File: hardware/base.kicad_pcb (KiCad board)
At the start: 4 copper layers, 100 x 85 mm, 296 parts, among them J101 USB-A, J102 TNG-Data-TOP, J103 TNG-Power-TOP, J301 MICROSDCARD, J302 Raspberry-Pi-Compute-Socket, J303 MICRO_HDMI, J304 USB Micro, J401 RJSLG-001TA1, P101 Debug, P102 Boot, P103 PE, P201 DI IN, P202 PWR IN, P301 XMC Flash, Q301 2N7002P, Q302 2N7002P, Q303 2N7002P, Q304 2N7002P, Q305 2N7002P, T201 744272251, U101 USB2517, U102 MIC2026-1YM, U103 82400152, U104 XMC1XXX24, U105 TPD4S010DQA, U106 TPD4S010DQA, U107 TPD4S010DQA, U108 AP7333-33SAG-7, U109 TPS22975, U110 TPS22975, U111 PCT2075DP, U112 VN7140AS, U201 ISO1211, U202 FPF2700MX, U203 BD90640HFP, U204 PAC1933, U301 PAM2306AYPAA, U302 PCF8523T, U303 FSUSB42MUX, U304 TPD4S010DQA, U305 TPD4S010DQA, U306 TPD4S010DQA, U307 82400152, U308 ATECC608A, U309 AP2331, U401 LAN7500, U402 93AA66, U403 TPD4S010DQA, U404 TPD4S010DQA, U405 PAM2306AYPAA, X101 24MHz, X301 32.768kHz, X401 25MHz

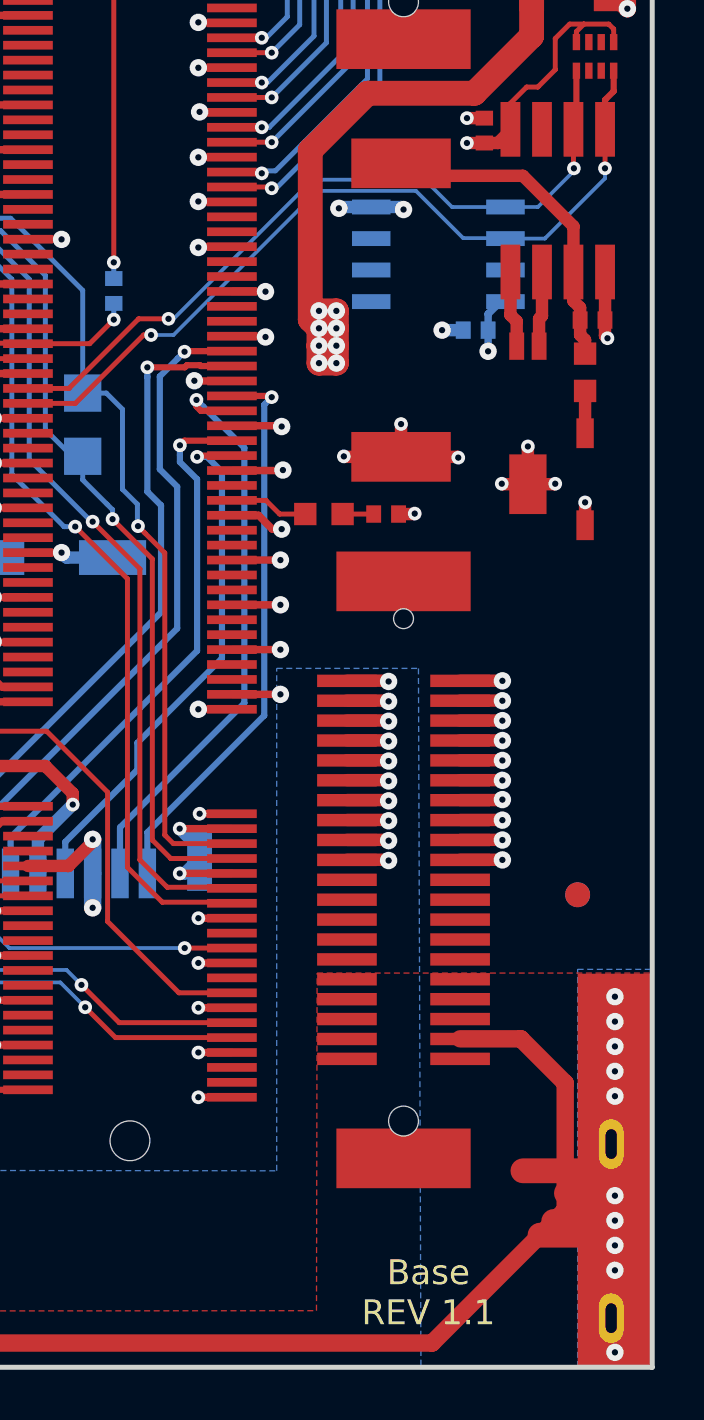
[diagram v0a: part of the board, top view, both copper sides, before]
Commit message: start version 1.2:
 * fix cryptochip i2c connections
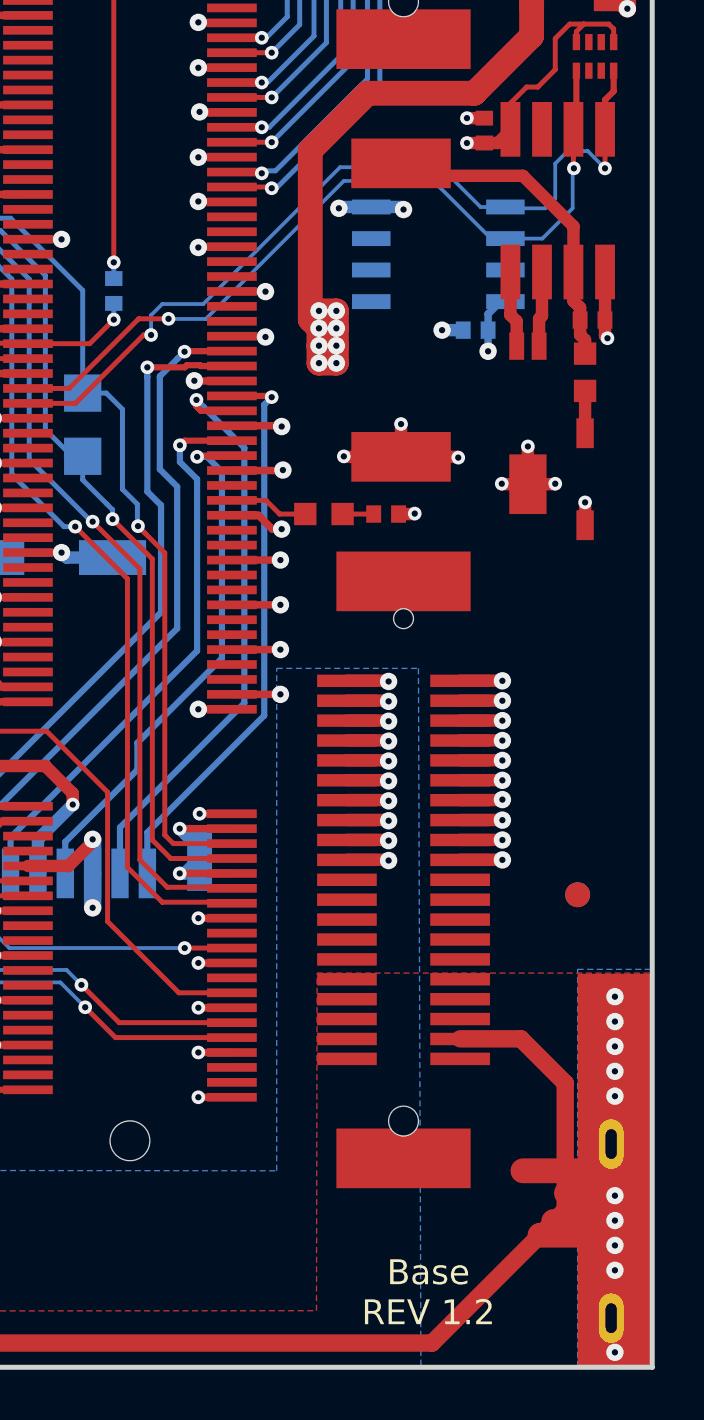
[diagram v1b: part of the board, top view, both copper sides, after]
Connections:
- J103 pad 21: (no net) -> Net-(J103-Pad21)
- J103 pad 22: (no net) -> Net-(J103-Pad22)
- J103 pad 23: (no net) -> Net-(J103-Pad23)
- J103 pad 24: (no net) -> Net-(J103-Pad24)
- J103 pad 25: (no net) -> Net-(J103-Pad25)
- J103 pad 26: (no net) -> Net-(J103-Pad26)
- J103 pad 27: (no net) -> Net-(J103-Pad27)
- J103 pad 28: (no net) -> Net-(J103-Pad28)
- J103 pad 29: (no net) -> Net-(J103-Pad29)
- J103 pad 30: (no net) -> Net-(J103-Pad30)
- J302 pad 10: (no net) -> Net-(J302-Pad10)
- J302 pad 100: (no net) -> Net-(J302-Pad100)
- J302 pad 101: (no net) -> Net-(J302-Pad101)
- J302 pad 102: (no net) -> Net-(J302-Pad102)
- J302 pad 105: (no net) -> Net-(J302-Pad105)
- J302 pad 106: (no net) -> Net-(J302-Pad106)
- J302 pad 107: (no net) -> Net-(J302-Pad107)
- J302 pad 108: (no net) -> Net-(J302-Pad108)
- J302 pad 112: (no net) -> Net-(J302-Pad112)
- J302 pad 114: (no net) -> Net-(J302-Pad114)
- J302 pad 118: (no net) -> Net-(J302-Pad118)
- J302 pad 12: (no net) -> Net-(J302-Pad12)
- J302 pad 120: (no net) -> Net-(J302-Pad120)
- J302 pad 124: (no net) -> Net-(J302-Pad124)
- J302 pad 126: (no net) -> Net-(J302-Pad126)
- J302 pad 128: (no net) -> Net-(J302-Pad128)
- J302 pad 130: (no net) -> Net-(J302-Pad130)
- J302 pad 132: (no net) -> Net-(J302-Pad132)
- J302 pad 135: (no net) -> Net-(J302-Pad135)
- J302 pad 136: (no net) -> Net-(J302-Pad136)
- J302 pad 137: (no net) -> Net-(J302-Pad137)
- J302 pad 138: (no net) -> Net-(J302-Pad138)
- J302 pad 141: (no net) -> Net-(J302-Pad141)
- J302 pad 142: (no net) -> Net-(J302-Pad142)
- J302 pad 143: (no net) -> Net-(J302-Pad143)
- J302 pad 144: (no net) -> Net-(J302-Pad144)
- J302 pad 147: (no net) -> Net-(J302-Pad147)
- J302 pad 148: (no net) -> Net-(J302-Pad148)
- J302 pad 149: (no net) -> Net-(J302-Pad149)
- J302 pad 150: (no net) -> Net-(J302-Pad150)
- J302 pad 153: (no net) -> Net-(J302-Pad153)
- J302 pad 154: (no net) -> Net-(J302-Pad154)
- J302 pad 155: (no net) -> Net-(J302-Pad155)
- J302 pad 156: (no net) -> Net-(J302-Pad156)
- J302 pad 158: (no net) -> Net-(J302-Pad158)
- J302 pad 159: (no net) -> Net-(J302-Pad159)
- J302 pad 16: (no net) -> Net-(J302-Pad16)
- J302 pad 160: (no net) -> Net-(J302-Pad160)
- J302 pad 161: (no net) -> Net-(J302-Pad161)
- J302 pad 162: (no net) -> Net-(J302-Pad162)
- J302 pad 166: (no net) -> Net-(J302-Pad166)
- J302 pad 17: (no net) -> Net-(J302-Pad17)
- J302 pad 172: (no net) -> Net-(J302-Pad172)
- J302 pad 174: (no net) -> Net-(J302-Pad174)
- J302 pad 176: (no net) -> Net-(J302-Pad176)
- J302 pad 177: (no net) -> Net-(J302-Pad177)
- J302 pad 178: (no net) -> Net-(J302-Pad178)
- J302 pad 179: (no net) -> Net-(J302-Pad179)
- J302 pad 18: (no net) -> Net-(J302-Pad18)
- J302 pad 180: (no net) -> Net-(J302-Pad180)
- J302 pad 22: (no net) -> Net-(J302-Pad22)
- J302 pad 23: (no net) -> Net-(J302-Pad23)
- J302 pad 24: (no net) -> Net-(J302-Pad24)
- J302 pad 3: (no net) -> Net-(J302-Pad3)
- J302 pad 34: (no net) -> Net-(J302-Pad34)
- J302 pad 36: (no net) -> Net-(J302-Pad36)
- J302 pad 4: (no net) -> Net-(J302-Pad4)
- J302 pad 45: (no net) -> Net-(J302-Pad45)
- J302 pad 46: (no net) -> Net-(J302-Pad46)
- J302 pad 47: (no net) -> Net-(J302-Pad47)
- J302 pad 48: (no net) -> Net-(J302-Pad48)
- J302 pad 5: (no net) -> Net-(J302-Pad5)
- J302 pad 51: (no net) -> Net-(J302-Pad51)
- J302 pad 52: (no net) -> Net-(J302-Pad52)
- J302 pad 53: (no net) -> Net-(J302-Pad53)
- J302 pad 54: (no net) -> Net-(J302-Pad54)
- J302 pad 57: (no net) -> Net-(J302-Pad57)
- J302 pad 58: (no net) -> Net-(J302-Pad58)
- J302 pad 59: (no net) -> Net-(J302-Pad59)
- J302 pad 6: (no net) -> Net-(J302-Pad6)
- J302 pad 60: (no net) -> Net-(J302-Pad60)
- J302 pad 63: (no net) -> Net-(J302-Pad63)
- J302 pad 64: (no net) -> Net-(J302-Pad64)
- J302 pad 65: (no net) -> Net-(J302-Pad65)
- J302 pad 66: (no net) -> Net-(J302-Pad66)
- J302 pad 70: (no net) -> Net-(J302-Pad70)
- J302 pad 71: (no net) -> Net-(J302-Pad71)
- J302 pad 72: (no net) -> Net-(J302-Pad72)
- J302 pad 76: (no net) -> Net-(J302-Pad76)
- J302 pad 78: (no net) -> Net-(J302-Pad78)
- J302 pad 93: (no net) -> Net-(J302-Pad93)
- J302 pad 94: (no net) -> Net-(J302-Pad94)
- J302 pad 95: (no net) -> Net-(J302-Pad95)
- J302 pad 96: (no net) -> Net-(J302-Pad96)
- J302 pad 99: (no net) -> Net-(J302-Pad99)
- J303 pad 2: (no net) -> Net-(J303-Pad2)
- J304 pad 4: (no net) -> Net-(J304-Pad4)
- P202 pad 1: (no net) -> Net-(P202-Pad1)
- R403 pad 1: (no net) -> Net-(R403-Pad1)
- RP101 pad 2: (no net) -> Net-(RP101-Pad2)
- RP101 pad 3: (no net) -> Net-(RP101-Pad3)
- RP101 pad 6: (no net) -> Net-(RP101-Pad6)
- RP101 pad 7: (no net) -> Net-(RP101-Pad7)
- RP102 pad 3: (no net) -> Net-(RP102-Pad3)
- RP102 pad 6: (no net) -> Net-(RP102-Pad6)
- RP302 pad 2: (no net) -> Net-(RP302-Pad2)
- RP302 pad 3: (no net) -> Net-(RP302-Pad3)
- RP302 pad 6: (no net) -> Net-(RP302-Pad6)
- RP302 pad 7: (no net) -> Net-(RP302-Pad7)
- RP303 pad 2: (no net) -> Net-(RP303-Pad2)
- RP303 pad 3: (no net) -> Net-(RP303-Pad3)
- RP303 pad 6: (no net) -> Net-(RP303-Pad6)
- RP303 pad 7: (no net) -> Net-(RP303-Pad7)
- U101 pad 14: (no net) -> Net-(U101-Pad14)
- U101 pad 15: (no net) -> Net-(U101-Pad15)
- U101 pad 16: (no net) -> Net-(U101-Pad16)
- U101 pad 18: (no net) -> Net-(U101-Pad18)
- U101 pad 20: (no net) -> Net-(U101-Pad20)
- U101 pad 21: (no net) -> Net-(U101-Pad21)
- U101 pad 22: (no net) -> Net-(U101-Pad22)
- U101 pad 23: (no net) -> Net-(U101-Pad23)
- U101 pad 26: (no net) -> Net-(U101-Pad26)
- U101 pad 27: (no net) -> Net-(U101-Pad27)
- U101 pad 28: (no net) -> Net-(U101-Pad28)
- U101 pad 29: (no net) -> Net-(U101-Pad29)
- U101 pad 30: (no net) -> Net-(U101-Pad30)
- U101 pad 31: (no net) -> Net-(U101-Pad31)
- U101 pad 32: (no net) -> Net-(U101-Pad32)
- U101 pad 33: (no net) -> Net-(U101-Pad33)
- U101 pad 34: (no net) -> Net-(U101-Pad34)
- U101 pad 35: (no net) -> Net-(U101-Pad35)
- U101 pad 36: (no net) -> Net-(U101-Pad36)
- U101 pad 37: (no net) -> Net-(U101-Pad37)
- U101 pad 47: (no net) -> Net-(U101-Pad47)
- U101 pad 48: (no net) -> Net-(U101-Pad48)
- U101 pad 49: (no net) -> Net-(U101-Pad49)
- U101 pad 50: (no net) -> Net-(U101-Pad50)
- U101 pad 51: (no net) -> Net-(U101-Pad51)
- U102 pad 3: (no net) -> Net-(U102-Pad3)
- U102 pad 5: (no net) -> Net-(U102-Pad5)
- U104 pad 6: (no net) -> Net-(U104-Pad6)
- U107 pad 1: (no net) -> Net-(U107-Pad1)
- U107 pad 10: (no net) -> Net-(U107-Pad10)
- U107 pad 2: (no net) -> Net-(U107-Pad2)
- U107 pad 9: (no net) -> Net-(U107-Pad9)
- U111 pad 3: (no net) -> Net-(U111-Pad3)
- U201 pad 5: (no net) -> Net-(U201-Pad5)
- U202 pad 2: (no net) -> Net-(U202-Pad2)
- U204 pad 10: (no net) -> Net-(U204-Pad10)
- U204 pad 9: (no net) -> Net-(U204-Pad9)
- U301 pad 11: (no net) -> Net-(U301-Pad11)
- U301 pad 5: (no net) -> Net-(U301-Pad5)
- U302 pad 7: (no net) -> Net-(U302-Pad7)
- U308 pad 1: (no net) -> Net-(U308-Pad1)
- U308 pad 2: (no net) -> Net-(U308-Pad2)
- U308 pad 3: (no net) -> Net-(U308-Pad3)
- U308 pad 5: Net-(J302-Pad84) -> Net-(J302-Pad82)
- U308 pad 6: Net-(J302-Pad82) -> Net-(J302-Pad84)
- U308 pad 7: (no net) -> Net-(U308-Pad7)
- U401 pad 10: (no net) -> Net-(U401-Pad10)
- U401 pad 18: (no net) -> Net-(U401-Pad18)
- U401 pad 21: (no net) -> Net-(U401-Pad21)
- U401 pad 22: (no net) -> Net-(U401-Pad22)
- U401 pad 25: (no net) -> Net-(U401-Pad25)
- U401 pad 31: (no net) -> Net-(U401-Pad31)
- U401 pad 32: (no net) -> Net-(U401-Pad32)
- U401 pad 35: (no net) -> Net-(U401-Pad35)
- U401 pad 38: (no net) -> Net-(U401-Pad38)
- U401 pad 4: (no net) -> Net-(U401-Pad4)
- U401 pad 40: (no net) -> Net-(U401-Pad40)
- U402 pad 6: (no net) -> Net-(U402-Pad6)
- U402 pad 7: (no net) -> Net-(U402-Pad7)
- U405 pad 10: (no net) -> Net-(U405-Pad10)
- U405 pad 11: (no net) -> Net-(U405-Pad11)
- U405 pad 2: (no net) -> Net-(U405-Pad2)
- U405 pad 5: (no net) -> Net-(U405-Pad5)
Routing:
- net Net-(J302-Pad84): track 30.6 -> 32.5 mm
- net Net-(J302-Pad82): track 33.0 -> 34.4 mm
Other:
- board text added: "Base REV 1.2"
- board text removed: "Base REV 1.1"

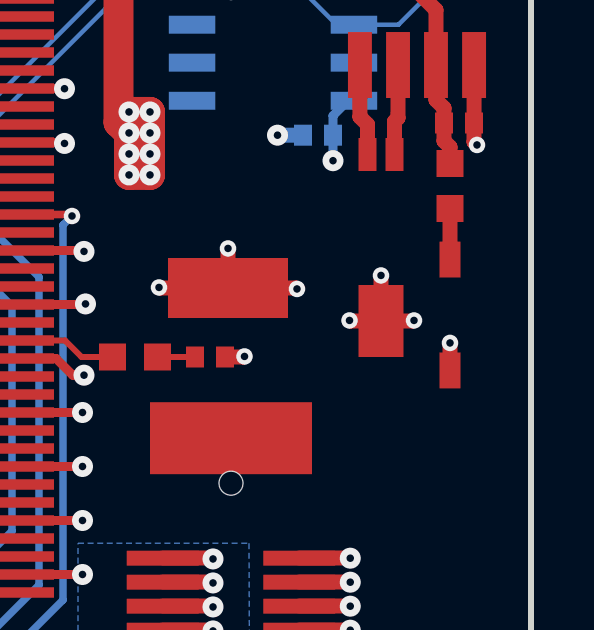
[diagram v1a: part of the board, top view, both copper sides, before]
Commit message: fix rtc diode
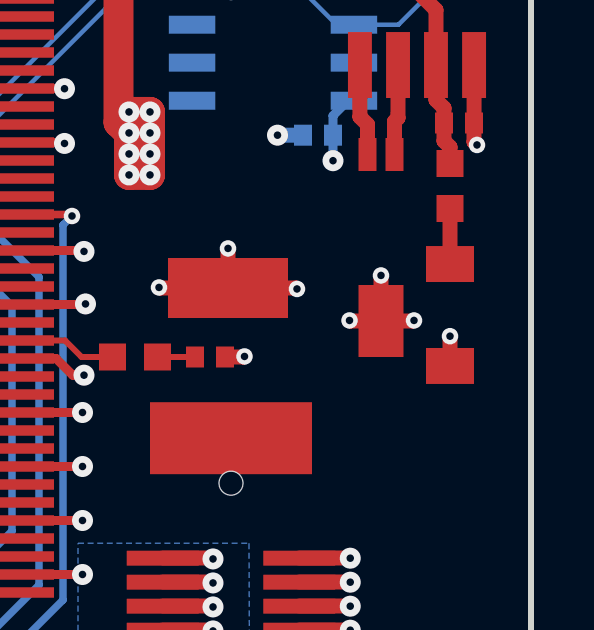
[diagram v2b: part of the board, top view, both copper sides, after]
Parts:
- D302: value B0520LW -> BAQ33-GS08; footprint SOD-123 -> kicad-libraries:MiniMelf
- turned D302 to 270 degrees

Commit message: change pcb silkscreen name
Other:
- board text added: "Base RPI CMX REV 1.2"
- board text removed: "Base REV 1.2"

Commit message: add remark
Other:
- board text added: "Testpunkte für Spannungen + GND auf Unterseite ATECC -> EEPROM + WP, Pogo Con TPM? SLB9670VQ20FW785XTMA1?"

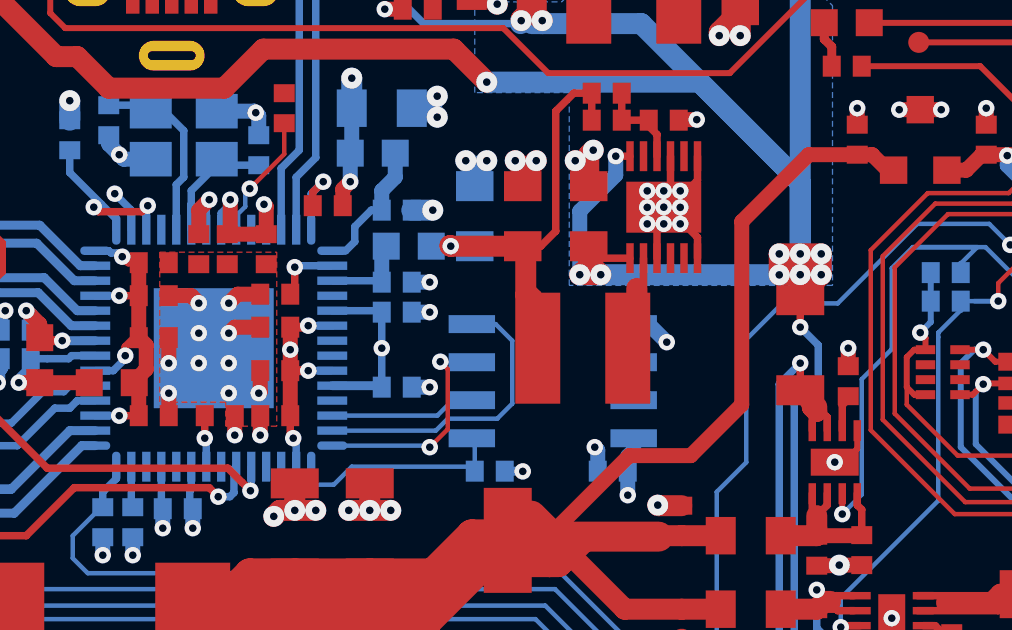
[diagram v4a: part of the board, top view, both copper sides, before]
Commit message: improve ethernet thermal design improve 1.2V generation
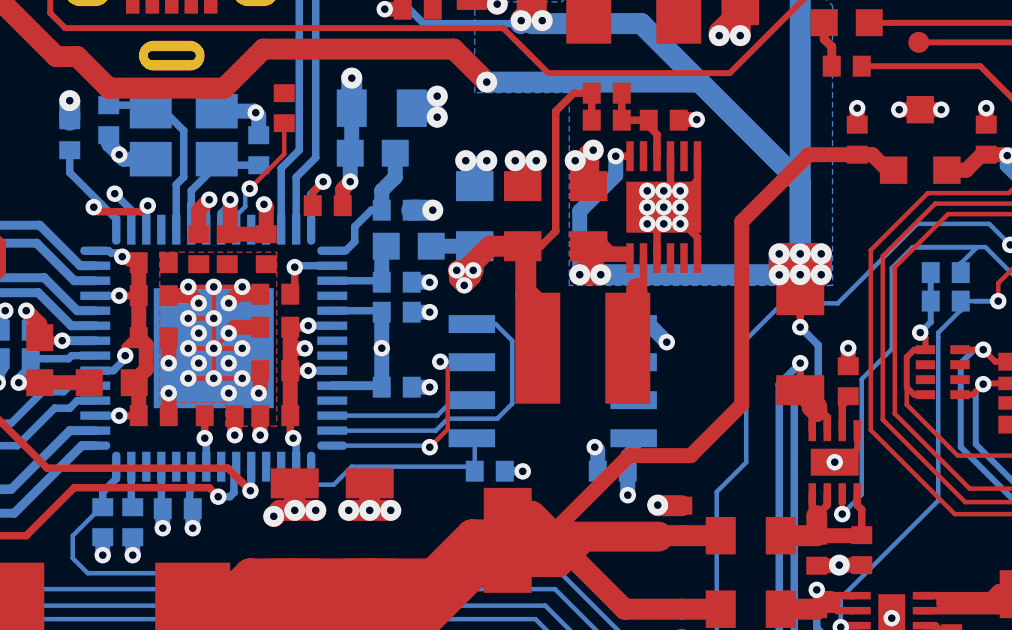
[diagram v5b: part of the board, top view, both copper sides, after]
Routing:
- net AGND: track 1052.5 -> 1062.5 mm, vias 545 -> 556
- net +1.2V: track 66.1 -> 73.7 mm, vias 9 -> 11
- net 5VSW: track 248.4 -> 251.9 mm
- net 3V3: track 459.9 -> 463.0 mm

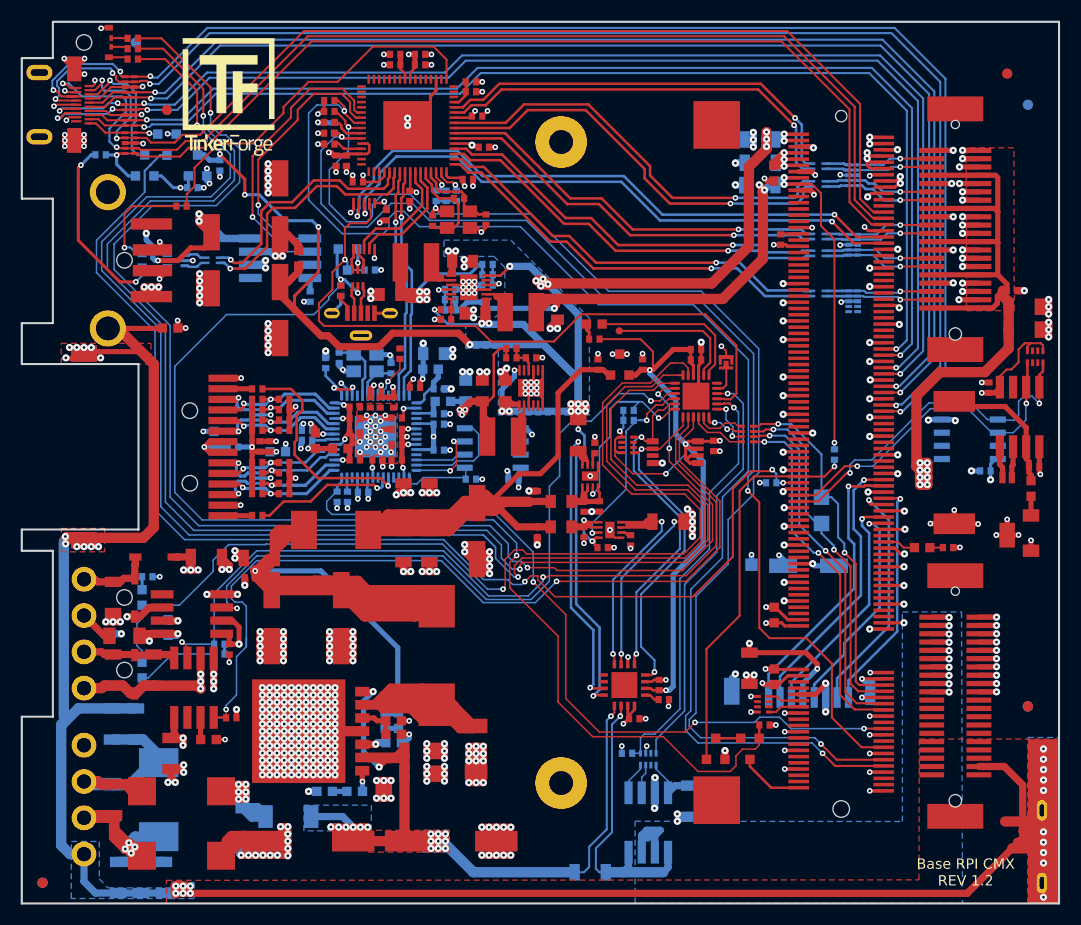
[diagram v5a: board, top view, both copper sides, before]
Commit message: add tpm module
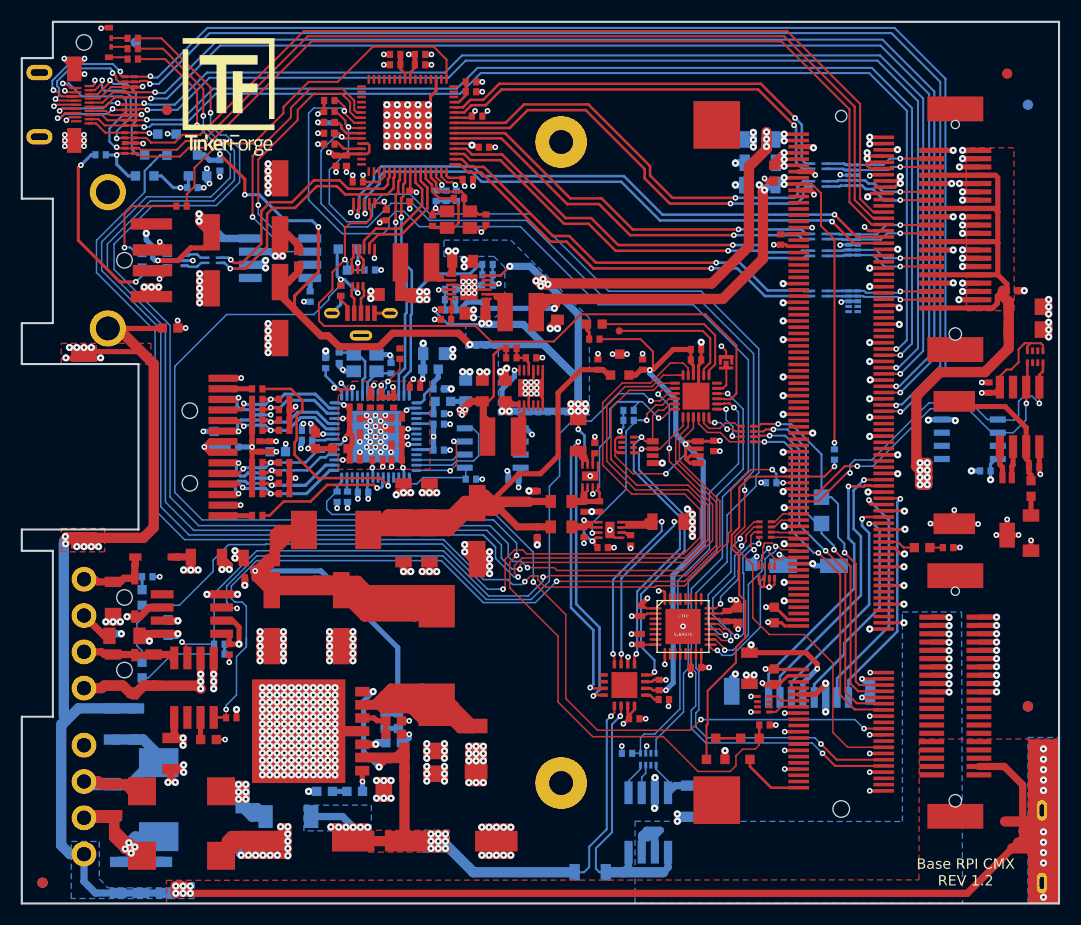
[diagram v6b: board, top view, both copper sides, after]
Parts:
- added C320: 1µF, C0603F, F.Cu at (126.5, 108.2)
- added C322: DNP, C0402F, F.Cu at (117.2, 107.8)
- added C323: 100nF, C0402F, F.Cu at (117.2, 110.5)
- added C324: DNP, C0402F, F.Cu at (122.5, 113.2)
- added C325: 100nF, C0402F, F.Cu at (125.3, 108.2)
- added RP304: 82, kicad-libraries:4X0402, F.Cu at (129.1, 99.9)
- added RP305: 10k, kicad-libraries:4X0402, F.Cu at (129.3, 104.0)
- added U310: SLB9670, kicad-libraries:QFN32-EXT, F.Cu at (121.2, 109.2)
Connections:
- J302 pad 64: Net-(J302-Pad64) -> TPM_IRQ
- J302 pad 66: Net-(J302-Pad66) -> TPM_RST
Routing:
- net AGND: track 1062.5 -> 1107.5 mm, vias 556 -> 589
- net 3V3: track 463.0 -> 501.0 mm, vias 46 -> 51
- net TPM_RST: track 0.00 -> 21.1 mm, vias 0 -> 2
- net TPM_IRQ: track 0.00 -> 18.4 mm, vias 0 -> 2
- net TPM_SCLK: track 0.00 -> 16.0 mm, vias 0 -> 2
- net TPM_CS: track 0.00 -> 16.0 mm, vias 0 -> 2
- net TPM_MOSI: track 0.00 -> 15.0 mm, vias 0 -> 2
- net TPM_MISO: track 0.00 -> 9.54 mm, vias 0 -> 2
- net Net-(J302-Pad78): track 0.00 -> 3.01 mm
- net Net-(J302-Pad76): track 0.00 -> 2.97 mm
- net Net-(J302-Pad70): track 0.00 -> 2.71 mm
- net Net-(J302-Pad72): track 0.00 -> 2.67 mm
- net Net-(J302-Pad88): track 116.1 -> 114.3 mm
- net RASP_USB_RESET: track 107.8 -> 109.6 mm
- net ORIG_USB_D+: track 58.4 -> 56.9 mm
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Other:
- board text added: "Testpunkte für Spannungen + GND auf Unterseite ATECC -> EEPROM + WP (nach außen), Pogo Con dafür mit WP nach außen TPM? SLB9670VQ20FW785XTMA1? SPI 2 Debug auf Unterseite als 0402 (DBG + GND)"
- board text removed: "Testpunkte für Spannungen + GND auf Unterseite ATECC -> EEPROM + WP, Pogo Con TPM? SLB9670VQ20FW785XTMA1?"
